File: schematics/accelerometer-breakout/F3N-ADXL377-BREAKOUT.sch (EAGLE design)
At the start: 8 parts

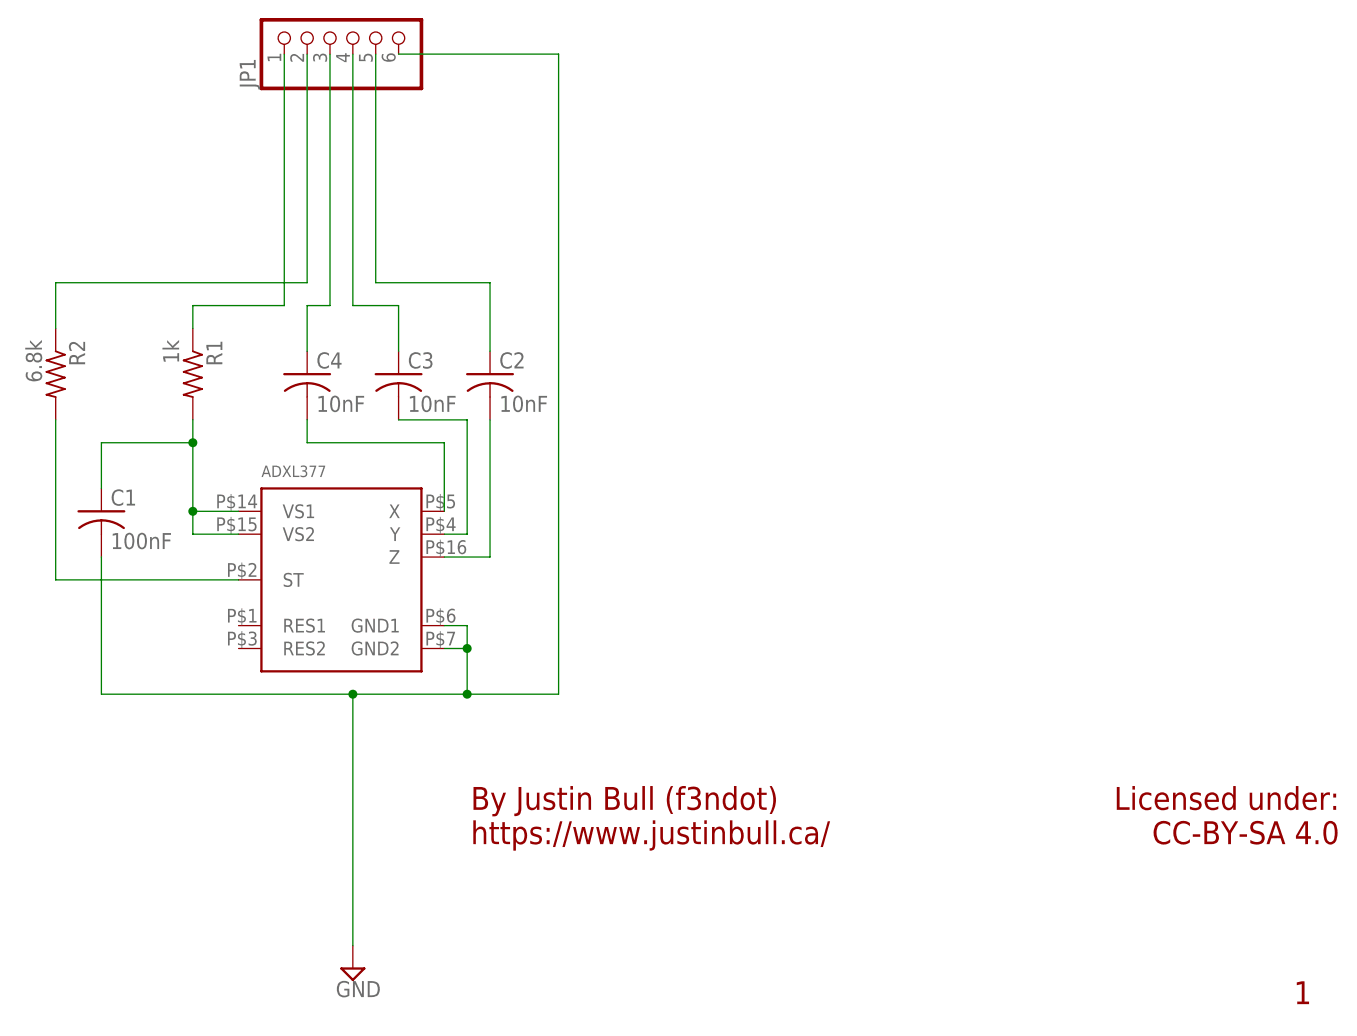
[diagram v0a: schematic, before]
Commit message: Routed, t/b GND plane, Cap parallel fix
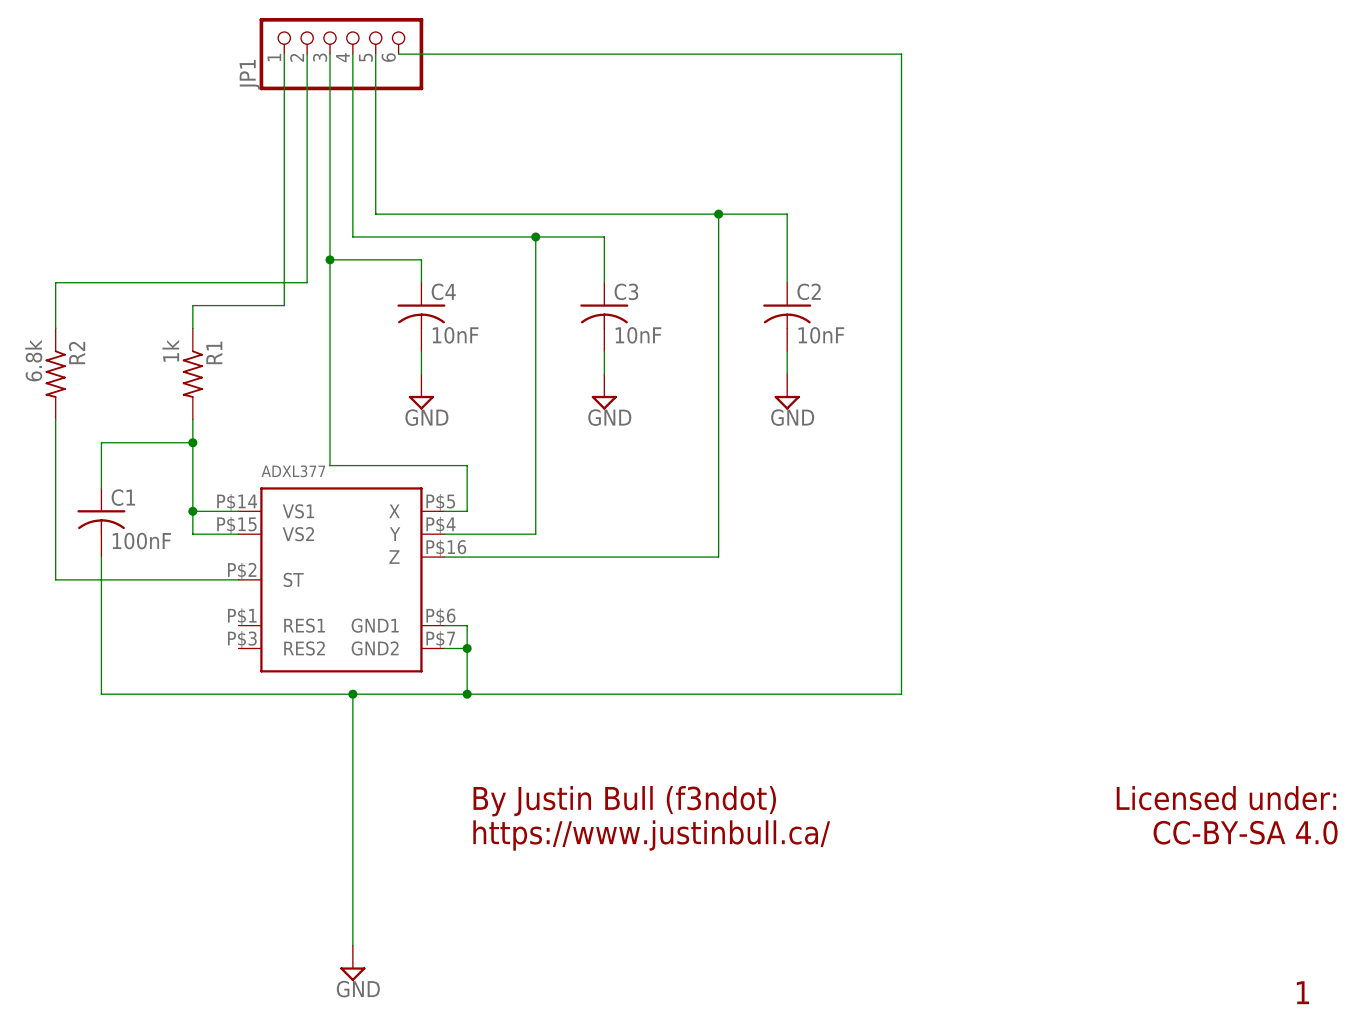
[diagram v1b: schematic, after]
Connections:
- net N$3 renamed VS
- net N$5 renamed ST
- removed net N$10: ADXL377.Y, C3.2
- removed net N$11: ADXL377.X, C4.2
- removed net N$2: C4.1, JP1.3
- removed net N$6: C3.1, JP1.4
- removed net N$7: C2.1, JP1.5
- removed net N$8: ADXL377.Z, C2.2
- new net X: ADXL377.X, C4.1, JP1.3
- new net Y: ADXL377.Y, C3.1, JP1.4
- new net Z: ADXL377.Z, C2.1, JP1.5
- net GND: now also C2.2, C3.2, C4.2
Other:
- moved on the sheet: C2, C3, C4
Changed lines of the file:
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@@
 <setting verticaltext="up"/>
 </settings>
-<grid distance="1" unitdist="mm" unit="mm" style="lines" multiple="1" display="yes" altdistance="0.05" altunitdist="inch" altunit="inch"/>
+<grid distance="0.1" unitdist="inch" unit="inch" style="lines" multiple="1" display="no" altdistance="0.01" altunitdist="inch" altunit="inch"/>
 <layers>
 <layer number="1" name="Top" color="4" fill="1" visible="no" active="no"/>
@@
 <part name="SUPPLY1" library="supply2" deviceset="GND" device=""/>
 <part name="FRAME1" library="frames" deviceset="FRAME_A_L" device=""/>
+<part name="SUPPLY2" library="supply2" deviceset="GND" device=""/>
+<part name="SUPPLY3" library="supply2" deviceset="GND" device=""/>
+<part name="SUPPLY4" library="supply2" deviceset="GND" device=""/>
 </parts>
 <sheets>
@@
 <instance part="ADXL377" gate="G$1" x="137.16" y="109.22"/>
 <instance part="C1" gate="G$1" x="109.22" y="119.38"/>
-<instance part="C2" gate="G$1" x="152.4" y="134.62"/>
-<instance part="C3" gate="G$1" x="142.24" y="134.62"/>
-<instance part="C4" gate="G$1" x="132.08" y="134.62"/>
+<instance part="C2" gate="G$1" x="185.42" y="142.24"/>
+<instance part="C3" gate="G$1" x="165.1" y="142.24"/>
+<instance part="C4" gate="G$1" x="144.78" y="142.24"/>
 <instance part="JP1" gate="A" x="137.16" y="172.72" rot="R90"/>
 <instance part="SUPPLY1" gate="GND" x="137.16" y="68.58"/>
 <instance part="FRAME1" gate="G$2" x="147.72" y="57"/>
+<instance part="SUPPLY2" gate="GND" x="165.1" y="132.08"/>
+<instance part="SUPPLY3" gate="GND" x="185.42" y="132.08"/>
+<instance part="SUPPLY4" gate="GND" x="144.78" y="132.08"/>
 </instances>
 <busses>
@@
 </segment>
 </net>
-<net name="N$3" class="0">
+<net name="VS" class="0">
 <segment>
 <pinref part="R1" gate="G$1" pin="1"/>
@@
 </segment>
 </net>
-<net name="N$5" class="0">
+<net name="ST" class="0">
 <segment>
 <pinref part="R2" gate="G$1" pin="1"/>
@@
 <pinref part="JP1" gate="A" pin="2"/>
 <wire x1="132.08" y1="144.78" x2="132.08" y2="170.18" width="0.1524" layer="91"/>
-</segment>
-</net>
-<net name="N$2" class="0">
-<segment>
-<pinref part="JP1" gate="A" pin="3"/>
-<wire x1="134.62" y1="170.18" x2="134.62" y2="142.24" width="0.1524" layer="91"/>
-<wire x1="134.62" y1="142.24" x2="132.08" y2="142.24" width="0.1524" layer="91"/>
-<pinref part="C4" gate="G$1" pin="1"/>
-<wire x1="132.08" y1="142.24" x2="132.08" y2="137.16" width="0.1524" layer="91"/>
-</segment>
-</net>
-<net name="N$6" class="0">
-<segment>
-<pinref part="JP1" gate="A" pin="4"/>
-<wire x1="137.16" y1="170.18" x2="137.16" y2="142.24" width="0.1524" layer="91"/>
-<wire x1="137.16" y1="142.24" x2="142.24" y2="142.24" width="0.1524" layer="91"/>
-<pinref part="C3" gate="G$1" pin="1"/>
-<wire x1="142.24" y1="142.24" x2="142.24" y2="137.16" width="0.1524" layer="91"/>
-</segment>
-</net>
-<net name="N$7" class="0">
-<segment>
-<pinref part="JP1" gate="A" pin="5"/>
-<wire x1="139.7" y1="170.18" x2="139.7" y2="144.78" width="0.1524" layer="91"/>
-<wire x1="139.7" y1="144.78" x2="152.4" y2="144.78" width="0.1524" layer="91"/>
-<pinref part="C2" gate="G$1" pin="1"/>
-<wire x1="152.4" y1="144.78" x2="152.4" y2="137.16" width="0.1524" layer="91"/>
-</segment>
-</net>
-<net name="N$8" class="0">
-<segment>
-<pinref part="C2" gate="G$1" pin="2"/>
-<pinref part="ADXL377" gate="G$1" pin="Z"/>
-<wire x1="152.4" y1="129.54" x2="152.4" y2="114.3" width="0.1524" layer="91"/>
-<wire x1="152.4" y1="114.3" x2="147.32" y2="114.3" width="0.1524" layer="91"/>
-</segment>
-</net>
-<net name="N$10" class="0">
-<segment>
-<pinref part="C3" gate="G$1" pin="2"/>
-<wire x1="142.24" y1="129.54" x2="149.86" y2="129.54" width="0.1524" layer="91"/>
-<pinref part="ADXL377" gate="G$1" pin="Y"/>
-<wire x1="149.86" y1="129.54" x2="149.86" y2="116.84" width="0.1524" layer="91"/>
-<wire x1="149.86" y1="116.84" x2="147.32" y2="116.84" width="0.1524" layer="91"/>
-</segment>
-</net>
-<net name="N$11" class="0">
-<segment>
-<pinref part="C4" gate="G$1" pin="2"/>
-<wire x1="132.08" y1="129.54" x2="132.08" y2="127" width="0.1524" layer="91"/>
-<wire x1="132.08" y1="127" x2="147.32" y2="127" width="0.1524" layer="91"/>
-<pinref part="ADXL377" gate="G$1" pin="X"/>
-<wire x1="147.32" y1="127" x2="147.32" y2="119.38" width="0.1524" layer="91"/>
 </segment>
 </net>
@@
 <junction x="137.16" y="99.06"/>
 <pinref part="JP1" gate="A" pin="6"/>
-<wire x1="142.24" y1="170.18" x2="160.02" y2="170.18" width="0.1524" layer="91"/>
-<wire x1="160.02" y1="170.18" x2="160.02" y2="99.06" width="0.1524" layer="91"/>
-<wire x1="160.02" y1="99.06" x2="149.86" y2="99.06" width="0.1524" layer="91"/>
+<wire x1="142.24" y1="170.18" x2="198.12" y2="170.18" width="0.1524" layer="91"/>
+<wire x1="198.12" y1="170.18" x2="198.12" y2="99.06" width="0.1524" layer="91"/>
+<wire x1="198.12" y1="99.06" x2="149.86" y2="99.06" width="0.1524" layer="91"/>
 <junction x="149.86" y="99.06"/>
 </segment>
-</net>
+<segment>
+<pinref part="C4" gate="G$1" pin="2"/>
+<pinref part="SUPPLY4" gate="GND" pin="GND"/>
+<wire x1="144.78" y1="134.62" x2="144.78" y2="137.16" width="0.1524" layer="91"/>
+</segment>
+<segment>
+<pinref part="C3" gate="G$1" pin="2"/>
+<pinref part="SUPPLY2" gate="GND" pin="GND"/>
+<wire x1="165.1" y1="134.62" x2="165.1" y2="137.16" width="0.1524" layer="91"/>
+</segment>
+<segment>
+<pinref part="C2" gate="G$1" pin="2"/>
+<pinref part="SUPPLY3" gate="GND" pin="GND"/>
+<wire x1="185.42" y1="134.62" x2="185.42" y2="137.16" width="0.1524" layer="91"/>
+</segment>
+</net>
+<net name="X" class="0">
+<segment>
+<pinref part="JP1" gate="A" pin="3"/>
+<wire x1="134.62" y1="170.18" x2="134.62" y2="147.32" width="0.1524" layer="91"/>
+<wire x1="134.62" y1="147.32" x2="134.62" y2="124.46" width="0.1524" layer="91"/>
+<wire x1="134.62" y1="124.46" x2="149.86" y2="124.46" width="0.1524" layer="91"/>
+<pinref part="ADXL377" gate="G$1" pin="X"/>
+<wire x1="149.86" y1="124.46" x2="149.86" y2="119.38" width="0.1524" layer="91"/>
+<wire x1="149.86" y1="119.38" x2="147.32" y2="119.38" width="0.1524" layer="91"/>
+<pinref part="C4" gate="G$1" pin="1"/>
+<wire x1="144.78" y1="144.78" x2="144.78" y2="147.32" width="0.1524" layer="91"/>
+<wire x1="144.78" y1="147.32" x2="134.62" y2="147.32" width="0.1524" layer="91"/>
+<junction x="134.62" y="147.32"/>
+</segment>
+</net>
+<net name="Y" class="0">
+<segment>
+<pinref part="JP1" gate="A" pin="4"/>
+<wire x1="137.16" y1="170.18" x2="137.16" y2="149.86" width="0.1524" layer="91"/>
+<wire x1="137.16" y1="149.86" x2="157.48" y2="149.86" width="0.1524" layer="91"/>
+<pinref part="ADXL377" gate="G$1" pin="Y"/>
+<wire x1="157.48" y1="149.86" x2="157.48" y2="116.84" width="0.1524" layer="91"/>
+<wire x1="157.48" y1="116.84" x2="147.32" y2="116.84" width="0.1524" layer="91"/>
+<pinref part="C3" gate="G$1" pin="1"/>
+<wire x1="165.1" y1="144.78" x2="165.1" y2="149.86" width="0.1524" layer="91"/>
+<wire x1="165.1" y1="149.86" x2="157.48" y2="149.86" width="0.1524" layer="91"/>
+<junction x="157.48" y="149.86"/>
+</segment>
+</net>
+<net name="Z" class="0">
+<segment>
+<pinref part="JP1" gate="A" pin="5"/>
+<wire x1="139.7" y1="170.18" x2="139.7" y2="152.4" width="0.1524" layer="91"/>
+<wire x1="139.7" y1="152.4" x2="177.8" y2="152.4" width="0.1524" layer="91"/>
+<pinref part="ADXL377" gate="G$1" pin="Z"/>
+<wire x1="177.8" y1="152.4" x2="177.8" y2="114.3" width="0.1524" layer="91"/>
+<wire x1="177.8" y1="114.3" x2="147.32" y2="114.3" width="0.1524" layer="91"/>
+<pinref part="C2" gate="G$1" pin="1"/>
+<wire x1="185.42" y1="144.78" x2="185.42" y2="152.4" width="0.1524" layer="91"/>
+<wire x1="185.42" y1="152.4" x2="177.8" y2="152.4" width="0.1524" layer="91"/>
+<junction x="177.8" y="152.4"/>
+</segment>
+</net>

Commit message: Change CC-BY-SA to CC BY-SA
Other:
- note added: "Licensed under: CC BY-SA 4.0"
- note removed: "Licensed under: CC-BY-SA 4.0"
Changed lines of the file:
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@@
 <text x="241.7" y="64.62" size="2.54" layer="94" font="vector">1</text>
 <text x="246.78" y="82.4" size="2.54" layer="94" font="vector" align="bottom-right">Licensed under:
-CC-BY-SA 4.0</text>
+CC BY-SA 4.0</text>
 <text x="150.26" y="82.4" size="2.54" layer="94" font="vector">By Justin Bull (f3ndot)
 https://www.justinbull.ca/</text>
